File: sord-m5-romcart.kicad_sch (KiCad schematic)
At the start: 5 parts, among them SW1 Choose ROM, U2 27C256, U3 74LS00

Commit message: Cleaning up little things
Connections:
- no-connect marks 11 -> 14
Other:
- note removed: "TODO: Fix symbol pinout to be A/B"
- note removed: "TODO: decode the ROM0/ROM1 selects into high address lines"
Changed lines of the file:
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@@
-		)
-	)
-	(text "TODO: Fix symbol pinout to be A/B "
-		(exclude_from_sim no)
-		(at 76.835 144.78 0)
-		(effects
-			(font
-				(size 1.27 1.27)
-			)
 		)
 	)
@@
 		(exclude_from_sim no)
 		(at 71.755 130.175 0)
-		(effects
-			(font
-				(size 1.27 1.27)
-			)
-		)
-	)
-	(text "TODO: decode the ROM0/ROM1 selects into high address lines"
-		(exclude_from_sim no)
-		(at 140.335 142.24 0)
 		(effects
 			(font
@@
 	)
 	(no_connect
+		(at 80.645 118.745)
+	)
+	(no_connect
+		(at 80.645 123.825)
+	)
+	(no_connect
+		(at 80.645 121.285)
+	)
+	(no_connect

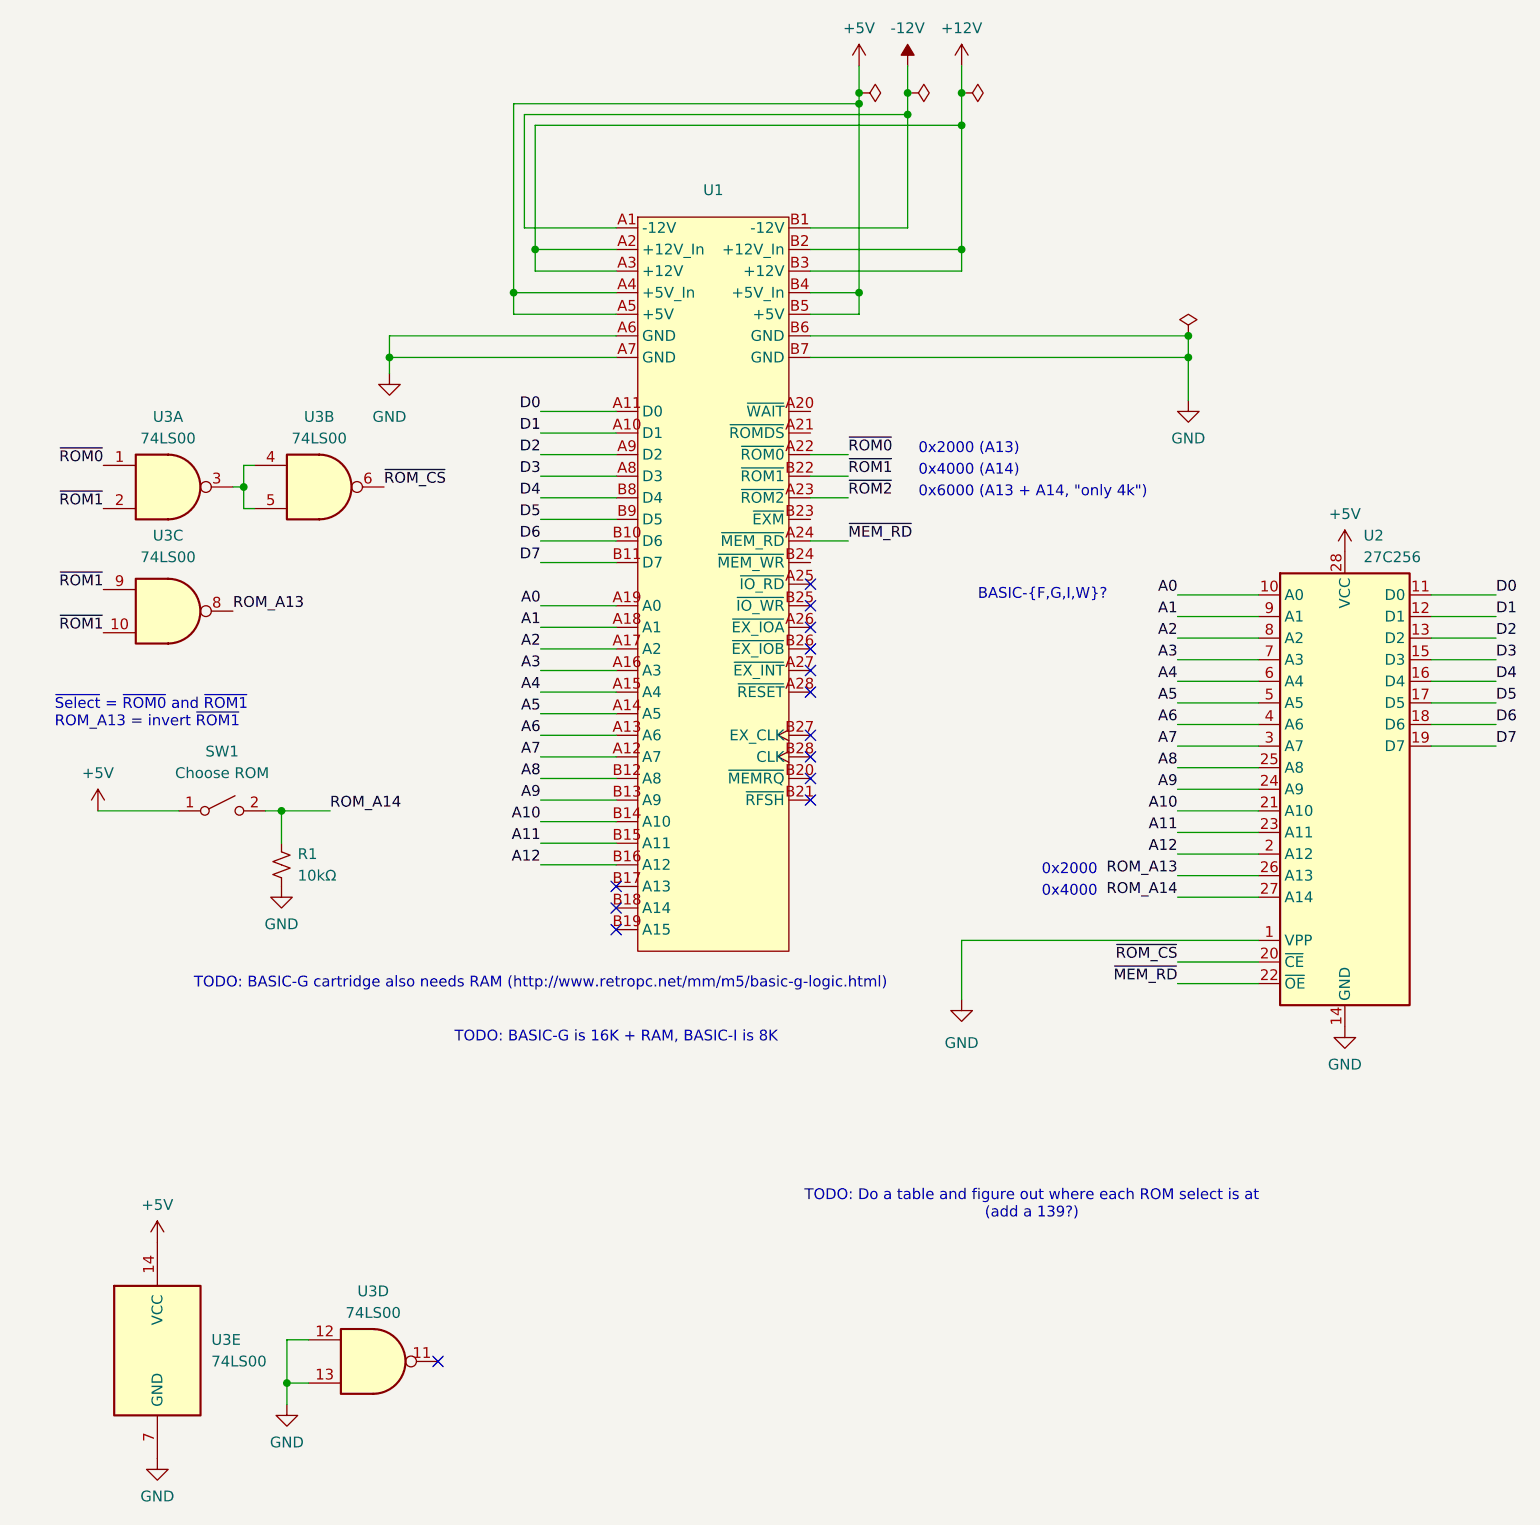
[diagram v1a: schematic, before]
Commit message: Converted to ROM1 base, re-routed
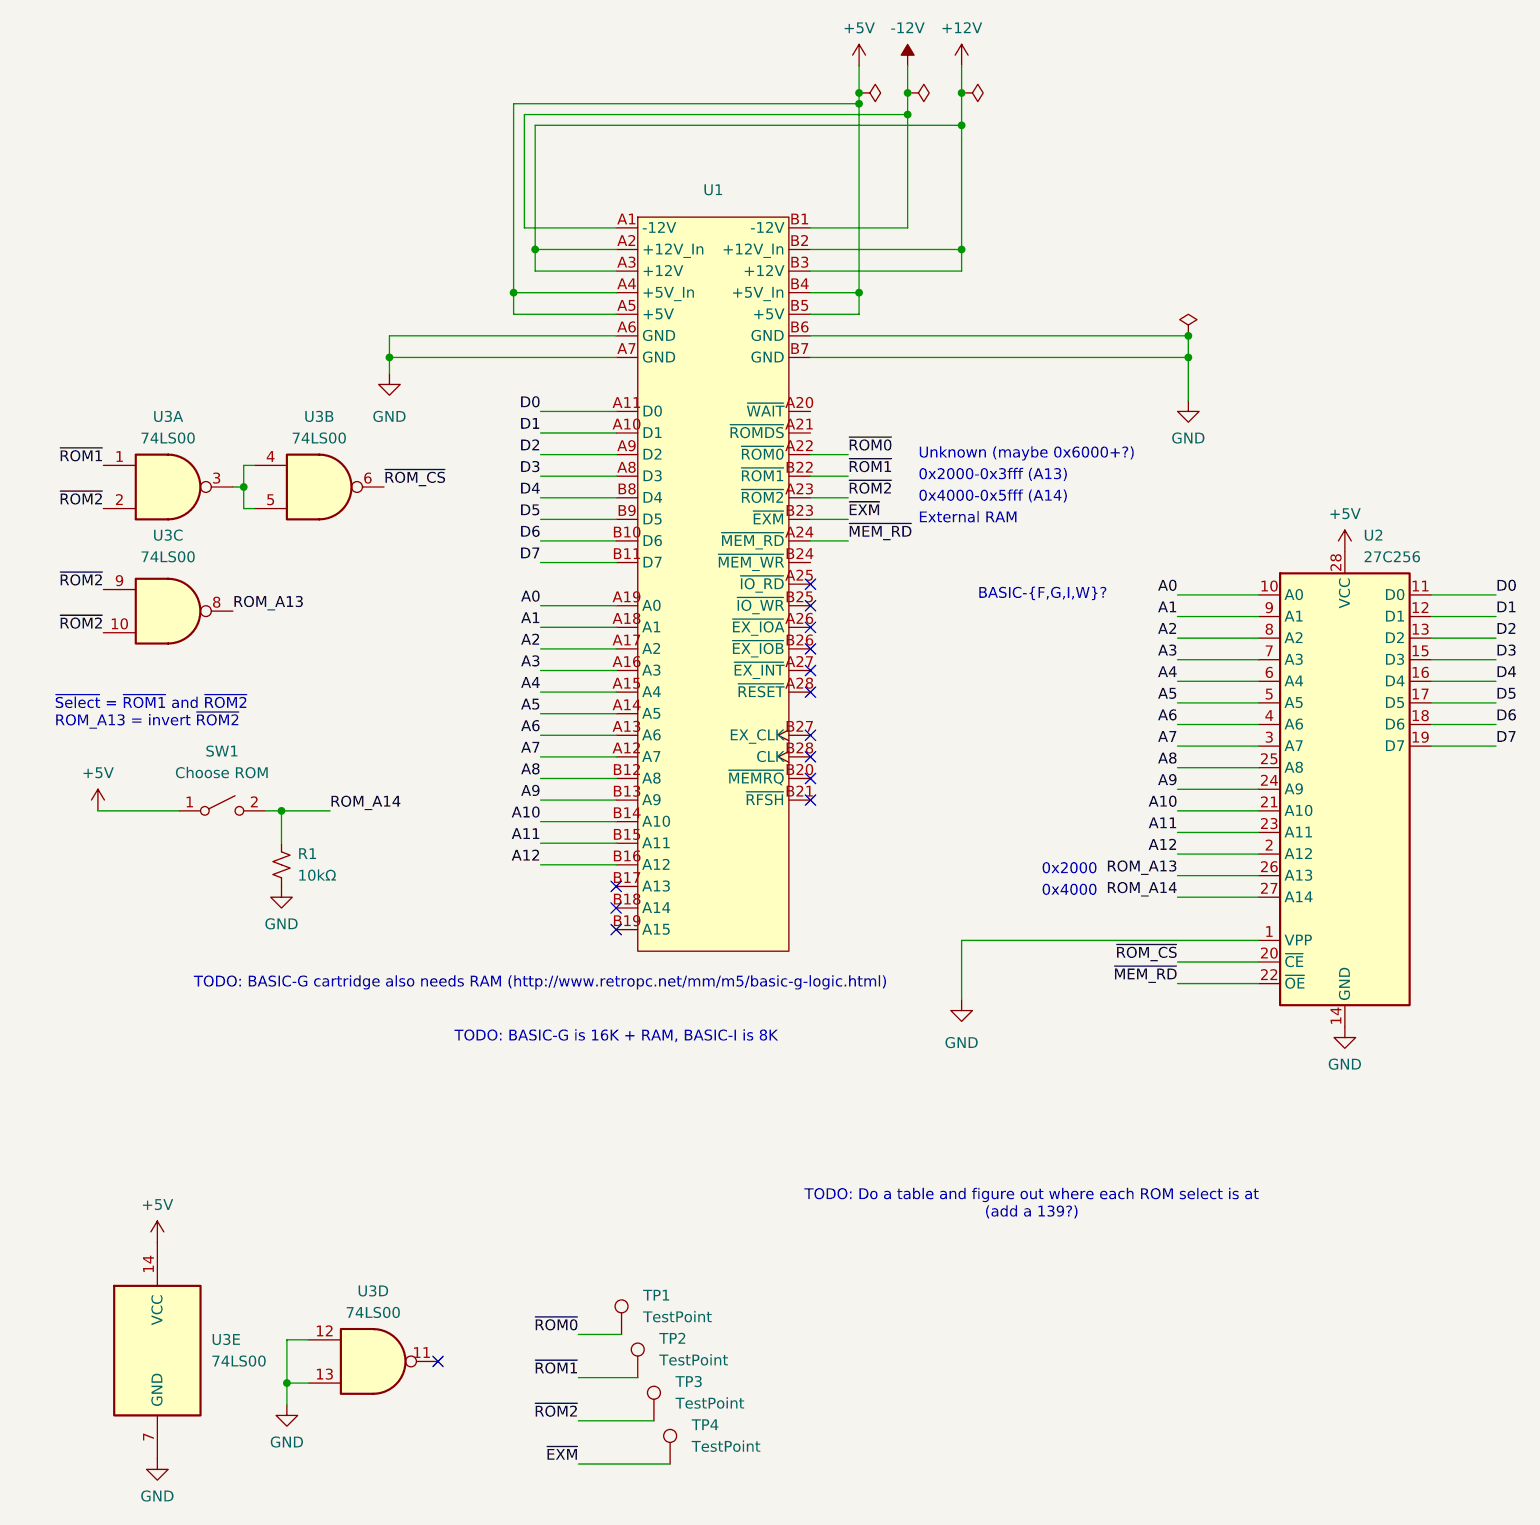
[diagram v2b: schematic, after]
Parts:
- added TP1, TP2, TP3, TP4: TestPoint, TestPoint:TestPoint_Loop_D1.80mm_Drill1.0mm_Beaded, symbol Connector:TestPoint
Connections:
- net ~{ROM0}: now also TP1.1; no longer U3.1
- net ~{ROM1}: now also U3.1, TP2.1; no longer U3.10, U3.2, U3.9
- net ~{ROM2}: now also U3.10, U3.2, U3.9, TP3.1
- net ~{EXM}: now reaches U1.B23 (~{EXM})
- net ~{EXM}: now also TP4.1
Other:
- note added: "0x2000-0x3fff (A13)"
- note added: "0x4000-0x5fff (A14)"
- note added: "External RAM"
- note added: "Unknown (maybe 0x6000+?)"
- note added: "~{Select} = ~{ROM1} and ~{ROM2} ROM_A13 = invert ~{ROM2}"
- note removed: "0x2000 (A13)"
- note removed: "0x4000 (A14)"
- note removed: "0x6000 (A13 + A14, "only 4k")"
- note removed: "~{Select} = ~{ROM0} and ~{ROM1} ROM_A13 = invert ~{ROM1}"

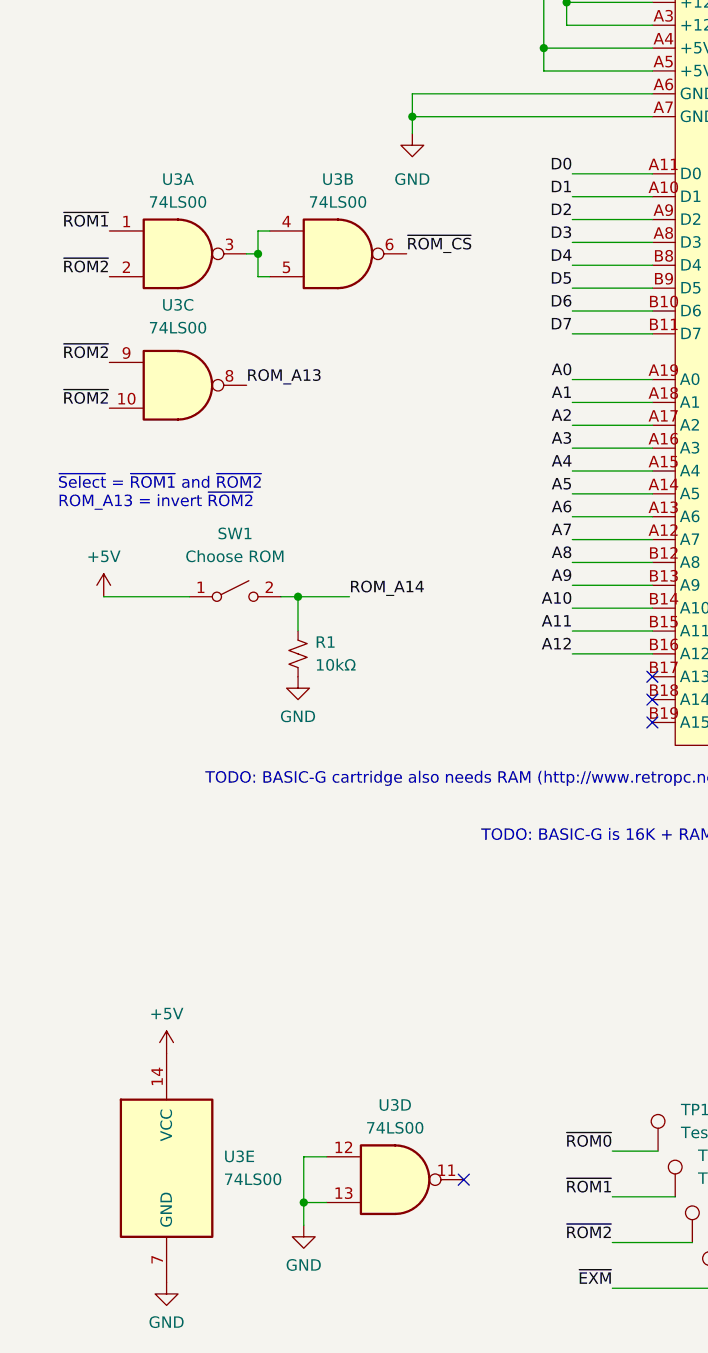
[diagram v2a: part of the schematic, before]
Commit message: Use AND not NAND
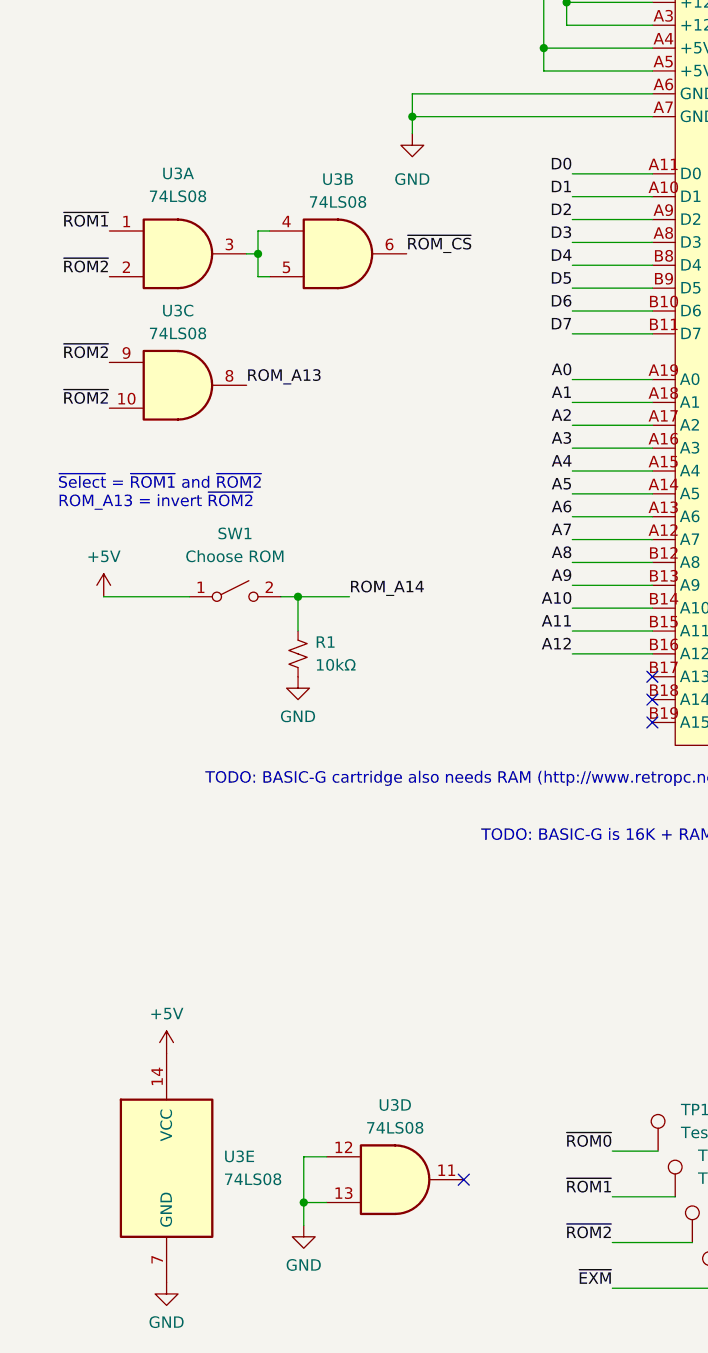
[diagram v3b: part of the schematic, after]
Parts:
- removed U3: 74LS00, Package_DIP:DIP-14_W7.62mm_Socket_LongPads, symbol 74xx:74LS00
- added U3: 74LS08, Package_DIP:DIP-14_W7.62mm_Socket_LongPads, symbol 74xx:74LS08
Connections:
- net +5V: now also U3.14 (VCC)
- net GND: now also U3.12, U3.13, U3.7 (GND)
- net ROM_A13: now also U3.8
- net ~{ROM1}: now also U3.1
- net ~{ROM2}: now also U3.10, U3.2, U3.9
- net ~{ROM_CS}: now also U3.6
- new net: U3.3, U3.4, U3.5

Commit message: Revert "Use AND not NAND"
This reverts commit 911c91f3a1e7fcb4d358834b32dfa7806c5ac1fb.
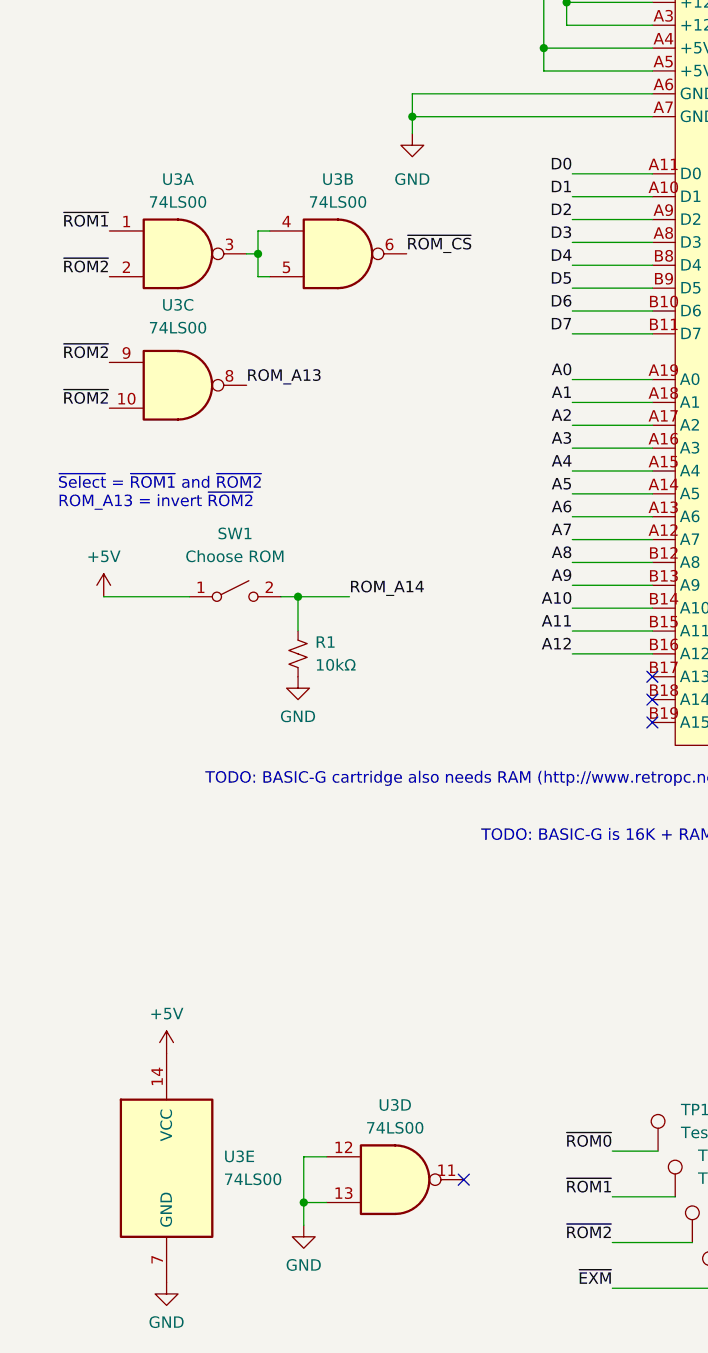
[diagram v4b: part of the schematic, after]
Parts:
- removed U3: 74LS08, Package_DIP:DIP-14_W7.62mm_Socket_LongPads, symbol 74xx:74LS08
- added U3: 74LS00, Package_DIP:DIP-14_W7.62mm_Socket_LongPads, symbol 74xx:74LS00
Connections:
- net +5V: now also U3.14 (VCC)
- net GND: now also U3.12, U3.13, U3.7 (GND)
- net ROM_A13: now also U3.8
- net ~{ROM1}: now also U3.1
- net ~{ROM2}: now also U3.10, U3.2, U3.9
- net ~{ROM_CS}: now also U3.6
- new net: U3.3, U3.4, U3.5
